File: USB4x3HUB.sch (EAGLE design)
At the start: 100 parts, among them IC10 IC_TTL_SINGLE_74_139_FLAT, IC6 3.3V, IC7 5V, IC8 5V, IC9 5V, J1 CON_DCJACK_C1604, Q1 48M/3225, SW1 RD, SW2 BL, SW3 GR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

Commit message: [ r0.3 ] library update
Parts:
- GIT1: value e64d5c4 -> 9ed6508
- IC10: value IC_TTL_SINGLE_74_139_FLAT -> SN74LVC1G139DCUR
- ICON2: device mylib:ICON_REVISION -> mylib:ICON_REVISION_2.0
- TP1, TP2: value TPPAD1-13 -> (none); device testpad_local:TPPAD1-13 -> mylib:TESTPAD_4020; NOT_COMPONENT YES -> (none)
- renumbered U$1 to GIT1
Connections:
- net GND: now also TP1.1, TP2.1; no longer TP1.TP, TP2.TP
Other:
- moved on the sheet: R27, R28, R29, R30
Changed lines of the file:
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@@
 <part name="R25" library="mylib" deviceset="R_US_*" device="_1005" technology="10K"/>
 <part name="R26" library="mylib" deviceset="R_US_*" device="_1005" technology="10K"/>
-<part name="IC10" library="mylib" deviceset="IC_TTL_SINGLE_74_139" device="_FLAT"/>
+<part name="IC10" library="mylib" deviceset="IC_TTL_SINGLE_74_139" device="_FLAT" value=" SN74LVC1G139DCUR"/>
 <part name="C20" library="mylib" deviceset="C_SMD_*" device="_1005" technology="0.1U"/>
 <part name="SUPPLY33" library="mylib" deviceset="GND" device=""/>
@@
 <part name="R32" library="mylib" deviceset="R_US_*" device="_1005" technology="10K"/>
 <part name="R31" library="mylib" deviceset="R_US_*" device="_1005" technology="10K"/>
-<part name="TP1" library="testpad_local" deviceset="TP" device="PAD1-13">
-<attribute name="NOT_COMPONENT" value="YES"/>
-</part>
-<part name="TP2" library="testpad_local" deviceset="TP" device="PAD1-13">
-<attribute name="NOT_COMPONENT" value="YES"/>
-</part>
 <part name="SUPPLY34" library="mylib" deviceset="GND" device=""/>
 <part name="SUPPLY35" library="mylib" deviceset="GND" device=""/>
@@
 <part name="TP102" library="mylib" deviceset="TESTPAD" device="_F"/>
 <part name="ICON1" library="mylib" deviceset="ICON_OSHW" device="" value="OSHW"/>
-<part name="ICON2" library="mylib" deviceset="ICON_REVISION" device="" value="r0.3"/>
-<part name="U$1" library="git-revision" deviceset="GIT-REVISION" device="" value="e64d5c4"/>
+<part name="ICON2" library="mylib" deviceset="ICON_REVISION" device="_2.0" value="r0.3"/>
 <part name="TP3" library="mylib" deviceset="TESTPAD" device=""/>
+<part name="GIT1" library="git-revision" deviceset="GIT-REVISION" device="" value="9ed6508"/>
+<part name="TP1" library="mylib" deviceset="TESTPAD" device="_4020"/>
+<part name="TP2" library="mylib" deviceset="TESTPAD" device="_4020"/>
 </parts>
 <sheets>
@@
 <wire x1="327.66" y1="165.1" x2="317.5" y2="165.1" width="0.1524" layer="94" style="shortdash"/>
 <text x="317.5" y="121.92" size="1.778" layer="94">15k/1005</text>
-<wire x1="332.74" y1="76.2" x2="350.52" y2="76.2" width="0.1524" layer="94" style="shortdash"/>
-<wire x1="350.52" y1="76.2" x2="350.52" y2="55.88" width="0.1524" layer="94" style="shortdash"/>
-<wire x1="350.52" y1="55.88" x2="332.74" y2="55.88" width="0.1524" layer="94" style="shortdash"/>
-<wire x1="332.74" y1="55.88" x2="332.74" y2="76.2" width="0.1524" layer="94" style="shortdash"/>
-<text x="335.28" y="53.34" size="1.778" layer="94">1k/1005</text>
+<wire x1="350.52" y1="76.2" x2="368.3" y2="76.2" width="0.1524" layer="94" style="shortdash"/>
+<wire x1="368.3" y1="76.2" x2="368.3" y2="55.88" width="0.1524" layer="94" style="shortdash"/>
+<wire x1="368.3" y1="55.88" x2="350.52" y2="55.88" width="0.1524" layer="94" style="shortdash"/>
+<wire x1="350.52" y1="55.88" x2="350.52" y2="76.2" width="0.1524" layer="94" style="shortdash"/>
+<text x="353.06" y="53.34" size="1.778" layer="94">1k/1005</text>
 <wire x1="157.48" y1="160.02" x2="170.18" y2="160.02" width="0.1524" layer="94" style="shortdash"/>
 <wire x1="170.18" y1="160.02" x2="170.18" y2="127" width="0.1524" layer="94" style="shortdash"/>
@@
 <instance part="C20" gate="G$1" x="302.26" y="81.28"/>
 <instance part="SUPPLY33" gate="GND" x="307.34" y="78.74" rot="R90"/>
-<instance part="LED1" gate="G$1" x="314.96" y="73.66" rot="R270"/>
-<instance part="LED2" gate="G$1" x="320.04" y="68.58" rot="R270"/>
-<instance part="LED3" gate="G$1" x="325.12" y="63.5" rot="R270"/>
-<instance part="LED4" gate="G$1" x="330.2" y="58.42" rot="R270"/>
-<instance part="R27" gate="G$1" x="342.9" y="73.66"/>
-<instance part="R28" gate="G$1" x="342.9" y="68.58"/>
-<instance part="R29" gate="G$1" x="342.9" y="63.5"/>
-<instance part="R30" gate="G$1" x="342.9" y="58.42"/>
+<instance part="LED1" gate="G$1" x="314.96" y="73.66" rot="R270">
+<attribute name="DIGIKEY" x="317.5" y="73.914" size="0.8128" layer="96" display="both"/>
+</instance>
+<instance part="LED2" gate="G$1" x="320.04" y="68.58" rot="R270">
+<attribute name="DIGIKEY" x="322.58" y="68.834" size="0.8128" layer="96" display="both"/>
+</instance>
+<instance part="LED3" gate="G$1" x="325.12" y="63.5" rot="R270">
+<attribute name="DIGIKEY" x="327.66" y="63.754" size="0.8128" layer="96" display="both"/>
+</instance>
+<instance part="LED4" gate="G$1" x="330.2" y="58.42" rot="R270">
+<attribute name="DIGIKEY" x="332.74" y="58.674" size="0.8128" layer="96" display="both"/>
+</instance>
+<instance part="R27" gate="G$1" x="360.68" y="73.66"/>
+<instance part="R28" gate="G$1" x="360.68" y="68.58"/>
+<instance part="R29" gate="G$1" x="360.68" y="63.5"/>
+<instance part="R30" gate="G$1" x="360.68" y="58.42"/>
 <instance part="R34" gate="G$1" x="200.66" y="93.98" rot="R90"/>
 <instance part="R33" gate="G$1" x="213.36" y="93.98" rot="R90"/>
 <instance part="R32" gate="G$1" x="226.06" y="93.98" rot="R90"/>
 <instance part="R31" gate="G$1" x="238.76" y="93.98" rot="R90"/>
-<instance part="TP1" gate="G$1" x="266.7" y="20.32">
-<attribute name="NOT_COMPONENT" x="266.7" y="20.32" size="1.778" layer="96" display="off"/>
-</instance>
-<instance part="TP2" gate="G$1" x="261.62" y="20.32">
-<attribute name="NOT_COMPONENT" x="261.62" y="20.32" size="1.778" layer="96" display="off"/>
-</instance>
 <instance part="SUPPLY34" gate="GND" x="261.62" y="15.24"/>
 <instance part="SUPPLY35" gate="GND" x="266.7" y="15.24"/>
@@
 <instance part="ICON1" gate="G$1" x="375.92" y="21.59"/>
 <instance part="ICON2" gate="G$1" x="289.56" y="5.08"/>
-<instance part="U$1" gate="G$1" x="342.9" y="20.32"/>
 <instance part="TP3" gate="1" x="170.18" y="111.76"/>
+<instance part="GIT1" gate="G$1" x="342.9" y="20.32"/>
+<instance part="TP1" gate="1" x="266.7" y="27.94" rot="R90"/>
+<instance part="TP2" gate="1" x="261.62" y="27.94" rot="R90"/>
 </instances>
 <busses>
@@
 </segment>
 <segment>
-<pinref part="TP2" gate="G$1" pin="TP"/>
 <pinref part="SUPPLY34" gate="GND" pin="GND"/>
-</segment>
-<segment>
-<pinref part="TP1" gate="G$1" pin="TP"/>
+<pinref part="TP2" gate="1" pin="1"/>
+<pinref part="TP2" gate="1" pin="1"/>
+<wire x1="261.62" y1="25.4" x2="261.62" y2="17.78" width="0.1524" layer="91"/>
+</segment>
+<segment>
 <pinref part="SUPPLY35" gate="GND" pin="GND"/>
+<pinref part="TP1" gate="1" pin="1"/>
+<pinref part="TP1" gate="1" pin="1"/>
+<wire x1="266.7" y1="25.4" x2="266.7" y2="17.78" width="0.1524" layer="91"/>
 </segment>
 <segment>
@@
 </segment>
 <segment>
-<wire x1="347.98" y1="81.28" x2="353.06" y2="81.28" width="0.1524" layer="91"/>
+<wire x1="365.76" y1="81.28" x2="370.84" y2="81.28" width="0.1524" layer="91"/>
 <pinref part="R27" gate="G$1" pin="2"/>
-<wire x1="345.44" y1="73.66" x2="347.98" y2="73.66" width="0.1524" layer="91"/>
-<wire x1="347.98" y1="73.66" x2="347.98" y2="81.28" width="0.1524" layer="91"/>
+<wire x1="363.22" y1="73.66" x2="365.76" y2="73.66" width="0.1524" layer="91"/>
+<wire x1="365.76" y1="73.66" x2="365.76" y2="81.28" width="0.1524" layer="91"/>
 <pinref part="R28" gate="G$1" pin="2"/>
-<wire x1="345.44" y1="68.58" x2="347.98" y2="68.58" width="0.1524" layer="91"/>
-<wire x1="347.98" y1="68.58" x2="347.98" y2="73.66" width="0.1524" layer="91"/>
-<junction x="347.98" y="73.66"/>
+<wire x1="363.22" y1="68.58" x2="365.76" y2="68.58" width="0.1524" layer="91"/>
+<wire x1="365.76" y1="68.58" x2="365.76" y2="73.66" width="0.1524" layer="91"/>
+<junction x="365.76" y="73.66"/>
 <pinref part="R29" gate="G$1" pin="2"/>
-<wire x1="345.44" y1="63.5" x2="347.98" y2="63.5" width="0.1524" layer="91"/>
-<wire x1="347.98" y1="63.5" x2="347.98" y2="68.58" width="0.1524" layer="91"/>
-<junction x="347.98" y="68.58"/>
+<wire x1="363.22" y1="63.5" x2="365.76" y2="63.5" width="0.1524" layer="91"/>
+<wire x1="365.76" y1="63.5" x2="365.76" y2="68.58" width="0.1524" layer="91"/>
+<junction x="365.76" y="68.58"/>
 <pinref part="R30" gate="G$1" pin="2"/>
-<wire x1="345.44" y1="58.42" x2="347.98" y2="58.42" width="0.1524" layer="91"/>
-<wire x1="347.98" y1="58.42" x2="347.98" y2="63.5" width="0.1524" layer="91"/>
-<junction x="347.98" y="63.5"/>
-<label x="350.52" y="81.28" size="1.778" layer="95"/>
+<wire x1="363.22" y1="58.42" x2="365.76" y2="58.42" width="0.1524" layer="91"/>
+<wire x1="365.76" y1="58.42" x2="365.76" y2="63.5" width="0.1524" layer="91"/>
+<junction x="365.76" y="63.5"/>
+<label x="368.3" y="81.28" size="1.778" layer="95"/>
 </segment>
 <segment>
@@
 <pinref part="LED4" gate="G$1" pin="A"/>
 <pinref part="R30" gate="G$1" pin="1"/>
-<wire x1="332.74" y1="58.42" x2="340.36" y2="58.42" width="0.1524" layer="91"/>
+<wire x1="332.74" y1="58.42" x2="358.14" y2="58.42" width="0.1524" layer="91"/>
 </segment>
 </net>
@@
 <pinref part="R29" gate="G$1" pin="1"/>
 <pinref part="LED3" gate="G$1" pin="A"/>
-<wire x1="340.36" y1="63.5" x2="327.66" y2="63.5" width="0.1524" layer="91"/>
+<wire x1="358.14" y1="63.5" x2="327.66" y2="63.5" width="0.1524" layer="91"/>
 </segment>
 </net>
@@
 <pinref part="LED2" gate="G$1" pin="A"/>
 <pinref part="R28" gate="G$1" pin="1"/>
-<wire x1="322.58" y1="68.58" x2="340.36" y2="68.58" width="0.1524" layer="91"/>
+<wire x1="322.58" y1="68.58" x2="358.14" y2="68.58" width="0.1524" layer="91"/>
 </segment>
 </net>
@@
 <pinref part="R27" gate="G$1" pin="1"/>
 <pinref part="LED1" gate="G$1" pin="A"/>
-<wire x1="340.36" y1="73.66" x2="317.5" y2="73.66" width="0.1524" layer="91"/>
-</segment>
-</net>
+<wire x1="358.14" y1="73.66" x2="317.5" y2="73.66" width="0.1524" layer="91"/>
+</segment>
+</net>

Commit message: [ r0.3 ] change NAME labels alignment to center; fix UART pins P0_0 and P0_4 must be used for UART as they are used by ISP
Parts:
- GIT1: value 9ed6508 -> 215f3cd
- IC1: value (none) -> TUSB2036
- IC2: value (none) -> FSUSB74MPX
- J1: value CON_DCJACK_C1604 -> (none)
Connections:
- removed net N$30: CON4.VCC
- net !OE!: now also U1.P0_13; no longer U1.P0_0/ACMP_I1
- net TGT_TX: now also U1.P0_0/ACMP_I1; no longer U1.P0_13
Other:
- note added: "!OE! = P0_13 SEL1 = P0_6 SEL0 = P0_7 TXT_TX = P0_0 TGT_RX = P0_4 SW1 = P0_8 SW2 = P0_1 SW3 = P0_9 SW4 = P0_10 1A=P0_3 1B=P0_2"
- note removed: "!OE! = P0_0 SEL1 = P0_6 SEL0 = P0_7 TXT_TX = P0_13 TGT_RX = P0_4 SW1 = P0_8 SW2 = P0_1 SW3 = P0_9 SW4 = P0_10 1A=P0_3 1B=P0_2"
- moved on the sheet: CON1, CON2, CON3, CON4, CON5, CON6, CON7, IC10, J1

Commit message: Revision 0.3
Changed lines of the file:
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@@
 <instance part="SUPPLY35" gate="GND" x="266.7" y="15.24"/>
 <instance part="SUPPLY32" gate="GND" x="226.06" y="124.46"/>
-<instance part="Q1" gate="G$1" x="162.56" y="119.38" smashed="yes">
-<attribute name="NAME" x="162.56" y="121.92" size="1.778" layer="95"/>
-<attribute name="VALUE" x="165.1" y="120.142" size="1.016" layer="96"/>
-</instance>
+<instance part="Q1" gate="G$1" x="162.56" y="119.38"/>
 <instance part="C21" gate="G$1" x="157.48" y="114.3" rot="MR0"/>
 <instance part="SUPPLY36" gate="GND" x="157.48" y="106.68"/>

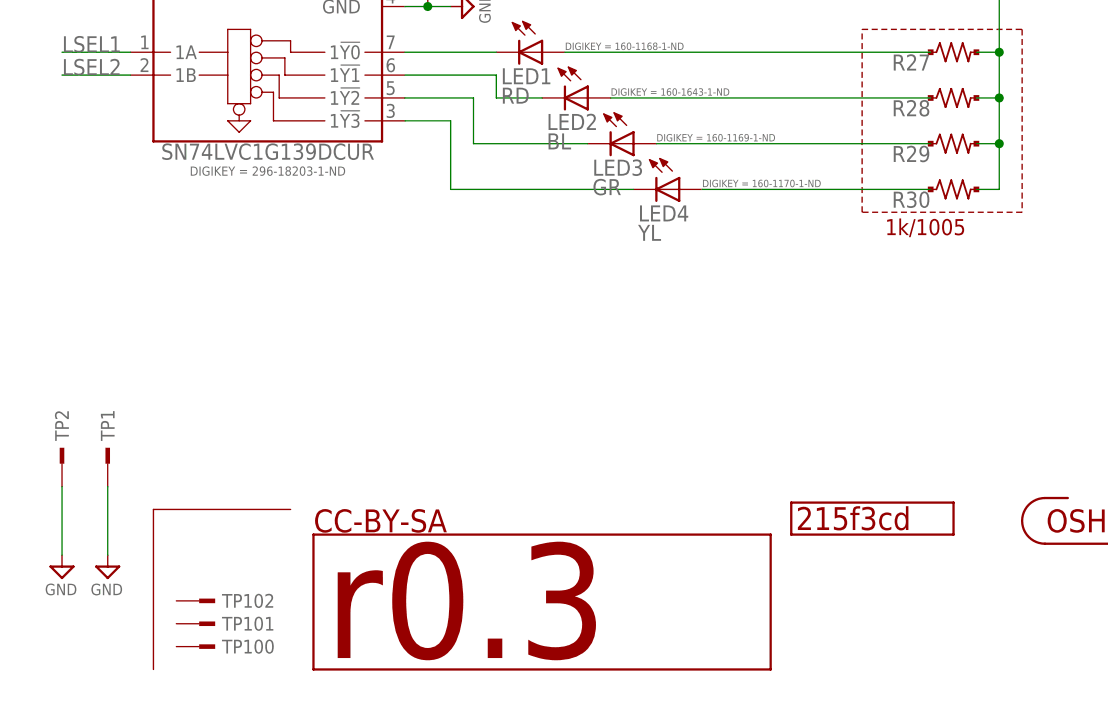
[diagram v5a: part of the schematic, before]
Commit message: library update: CON1-4 milling and IC10 attribute
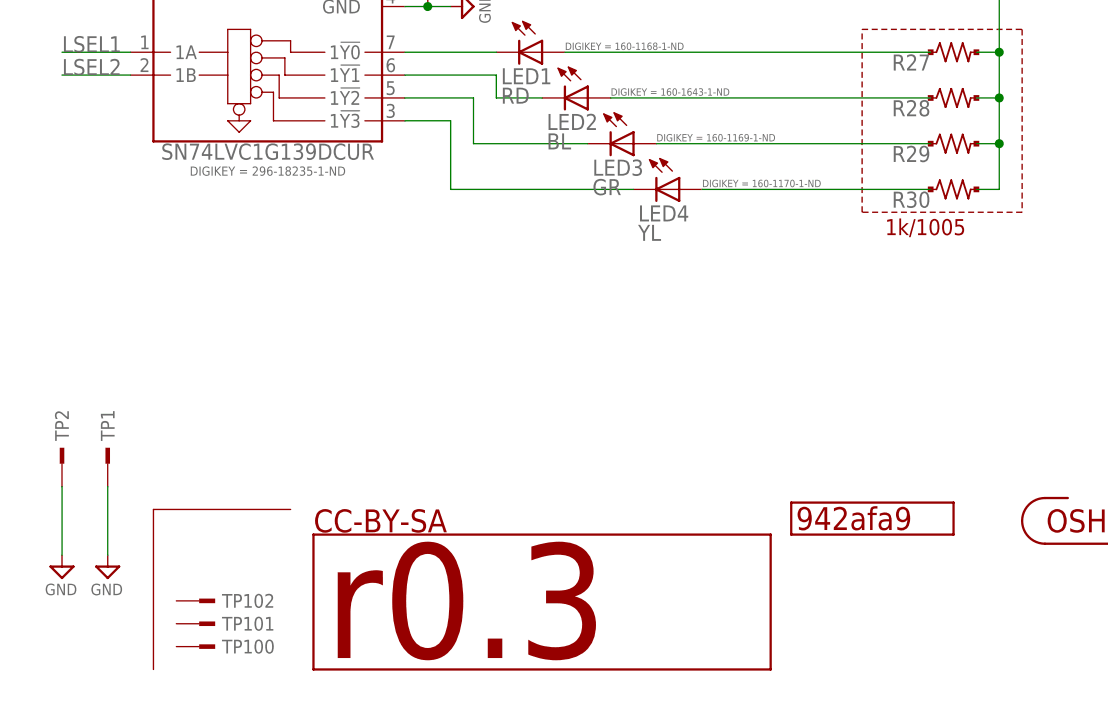
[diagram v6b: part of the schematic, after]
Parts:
- GIT1: value 215f3cd -> 942afa9
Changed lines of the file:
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@@
 <part name="ICON2" library="mylib" deviceset="ICON_REVISION" device="_2.0" value="r0.3"/>
 <part name="TP3" library="mylib" deviceset="TESTPAD" device=""/>
-<part name="GIT1" library="git-revision" deviceset="GIT-REVISION" device="" value="215f3cd"/>
+<part name="GIT1" library="git-revision" deviceset="GIT-REVISION" device="" value="942afa9"/>
 <part name="TP1" library="mylib" deviceset="TESTPAD" device="_4020"/>
 <part name="TP2" library="mylib" deviceset="TESTPAD" device="_4020"/>

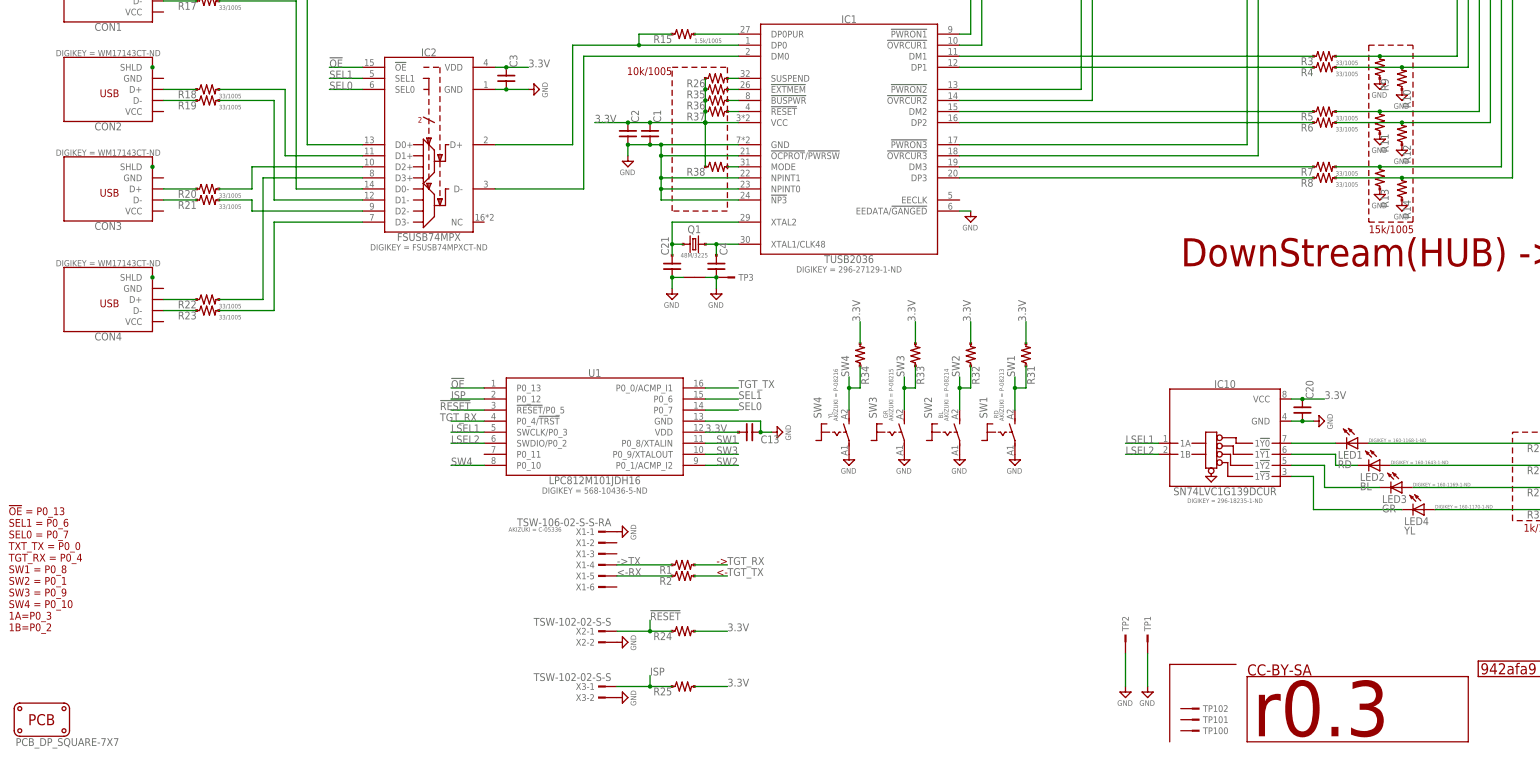
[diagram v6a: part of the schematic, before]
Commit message: replace Q1 to use Oscillator add R39~45; add TP3; remove C21
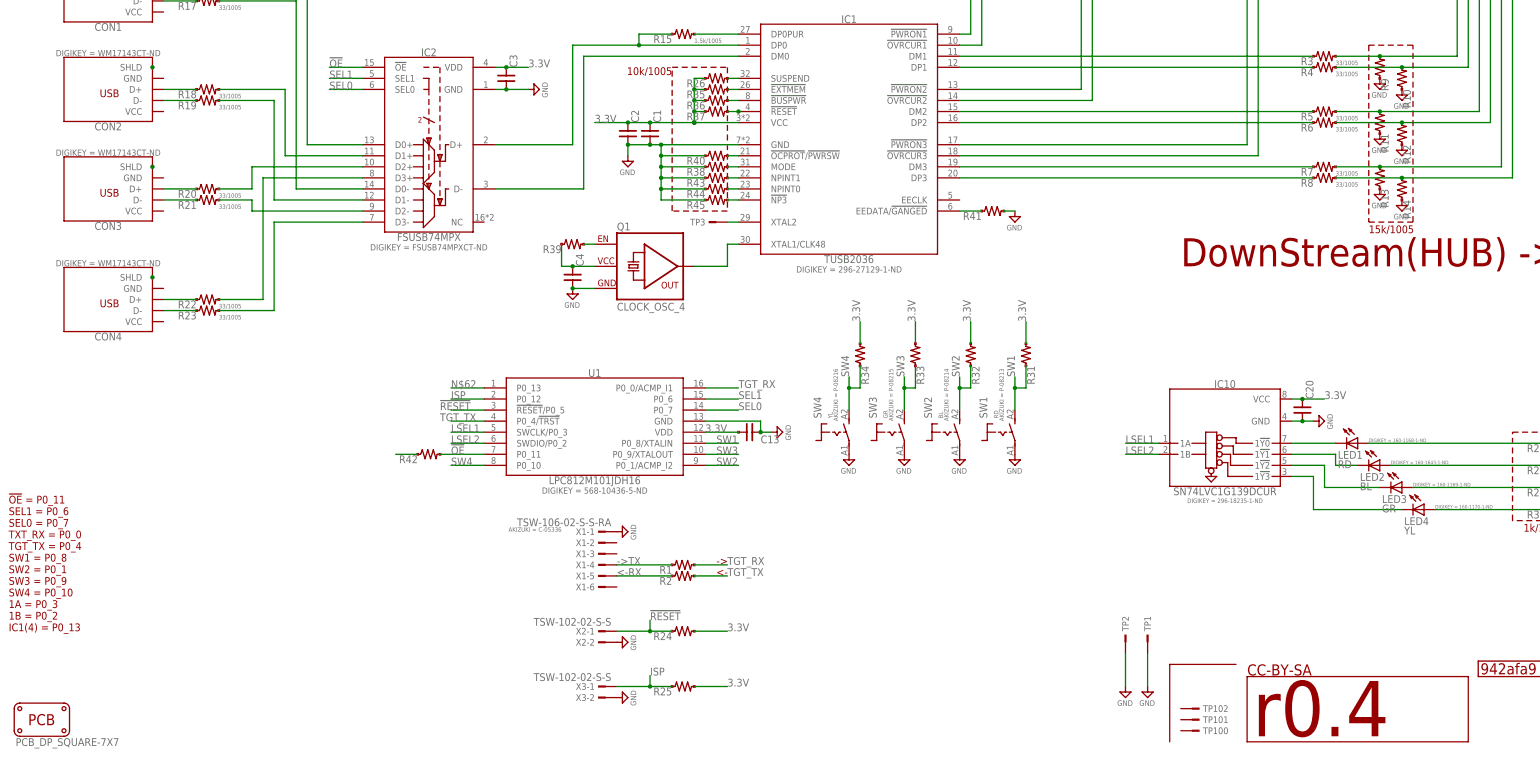
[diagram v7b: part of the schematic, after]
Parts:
- removed C21: (no value), mylib:C_SMD_18P_1005
- added R39, R40, R41, R42, R43, R44, R45: (no value), mylib:R_US_10K_1005
- C4: device mylib:C_SMD_18P_1005 -> mylib:C_SMD_0.1U_1005
- ICON2: value r0.3 -> r0.4
- Q1: value 48M/3225 -> CLOCK_OSC_4; device mylib:CRYSTAL4_48M_3225 -> mylib:CLOCK_OSC_4
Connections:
- new net N$30: IC1.EEDATA/!GANGED!, R41.1
- new net N$64: IC1.!OCPROT!/!PWRSW!, R40.2
- new net N$65: IC1.!NP3!, R45.2
- new net N$66: IC1.NPINT0, R44.2
- new net N$67: IC1.NPINT1, R43.2
- new net N$68: Q1.C, R39.2
- net !OE!: now also R42.2, U1.P0_11; no longer U1.P0_13
- net 3.3V: now also C4.1, Q1.VCC@2, R39.1, R42.1; no longer R38.1
- net GND: now also Q1.GND@1, R38.1, R40.1, R41.2, R43.1, R44.1, R45.1; no longer C21.2, IC1.!NP3!, IC1.!OCPROT!/!PWRSW!, IC1.EEDATA/!GANGED!, IC1.NPINT0, IC1.NPINT1, Q1.P$1, Q1.P$2, TP3.1
- net N$15: now also Q1.OUT@1; no longer C4.1, Q1.2
- net N$59: now also TP3.1; no longer C21.1, Q1.1
- net N$62: now also U1.P0_13
- net TGT_RX: now also U1.P0_0/ACMP_I1; no longer U1.P0_4/!TRST!
- net TGT_TX: now also U1.P0_4/!TRST!; no longer U1.P0_0/ACMP_I1
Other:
- note added: "!OE! = P0_11 SEL1 = P0_6 SEL0 = P0_7 TXT_RX = P0_0 TGT_TX = P0_4 SW1 = P0_8 SW2 = P0_1 SW3 = P0_9 SW4 = P0_10 1A = P0_3 1B = P0_2 IC1(4) = P0_13"
- note removed: "!OE! = P0_13 SEL1 = P0_6 SEL0 = P0_7 TXT_TX = P0_0 TGT_RX = P0_4 SW1 = P0_8 SW2 = P0_1 SW3 = P0_9 SW4 = P0_10 1A=P0_3 1B=P0_2"
- moved on the sheet: C4, TP3
